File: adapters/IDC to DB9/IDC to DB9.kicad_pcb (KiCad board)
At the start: 2 copper layers, 22.9 x 18.4 mm, 2 parts, among them J1 JoyKEY, J2 DB9

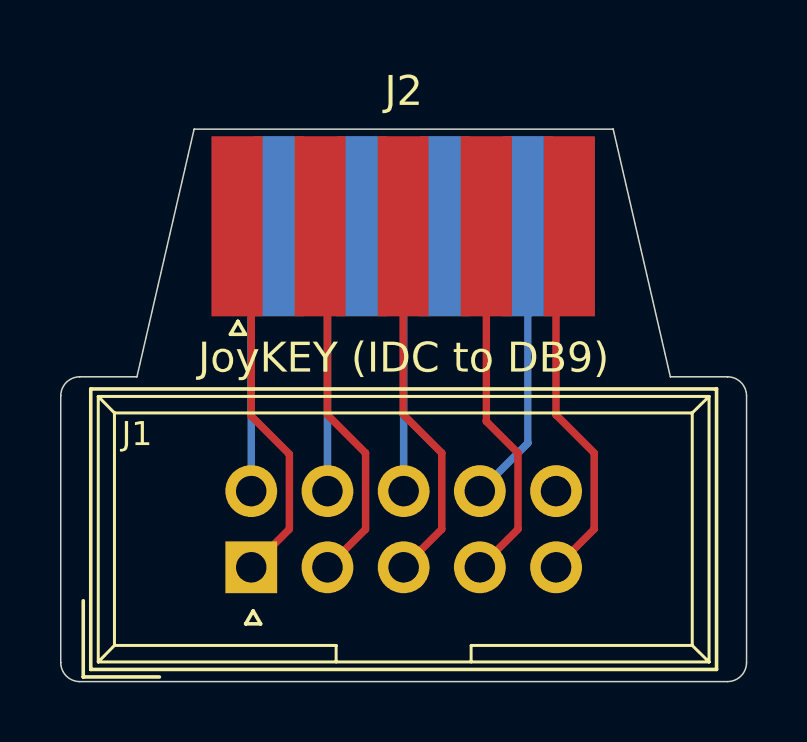
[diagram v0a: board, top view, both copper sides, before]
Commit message: Added VCC_EN to IDC -> DB9 adapter
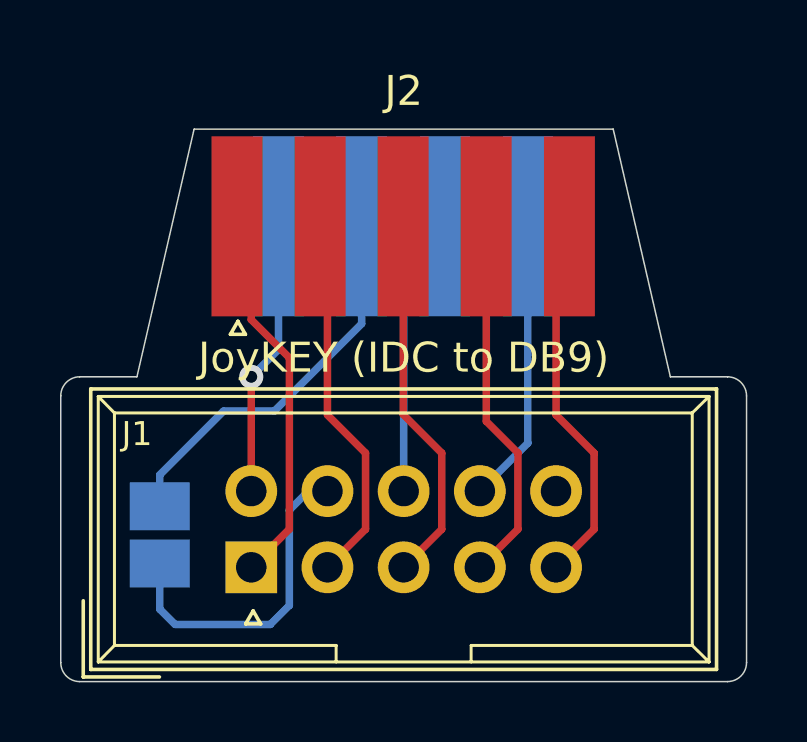
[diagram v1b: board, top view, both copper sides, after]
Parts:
- added JP1: PWR, solder_bridge:bridge, B.Cu at (134.1, 89.4)
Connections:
- J1 pad 7: VCC -> Net-(J1-Pad7)
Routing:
- net Net-(J1-Pad7): track 0.00 -> 11.0 mm
- net VCC: track 9.30 -> 13.1 mm
- net /FIRE1: vias 0 -> 1
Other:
- board text added: "VCC_EN"
- board text removed: "JoyKEY"
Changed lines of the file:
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@@
     (thickness 1.6)
     (drawings 15)
-    (tracks 31)
+    (tracks 43)
     (zones 0)
-    (modules 2)
-    (nets 10)
+    (modules 3)
+    (nets 11)
   )
   (page A4)
@@
   (net 8 /FIRE1)
   (net 9 /FIRE3)
+  (net 10 "Net-(J1-Pad7)")
   (net_class Default "This is the default net class."
     (clearance 0.2)
@@
     (add_net /UP)
     (add_net GND)
+    (add_net "Net-(J1-Pad7)")
     (add_net VCC)
   )
@@
       (net 1 GND))
     (pad 7 thru_hole oval (at 2.54 2.54 90) (size 1.7272 1.7272) (drill 1.016) (layers *.Cu *.Mask)
-      (net 7 VCC))
+      (net 10 "Net-(J1-Pad7)"))
     (pad 6 thru_hole oval (at 2.54 0 90) (size 1.7272 1.7272) (drill 1.016) (layers *.Cu *.Mask)
       (net 8 /FIRE1))
@@
     )
   )
+  (module solder_bridge:bridge (layer B.Cu)
+    (at 134.112 89.408)
+    (descr "Through hole straight pin header, 1x02, 1.00mm pitch, single row")
+    (tags "Through hole pin header THT 1x02 1.00mm single row")
+    (fp_text reference JP1 (at 0 2.54) (layer B.SilkS) hide
+      (effects (font (size 1 1) (thickness 0.15)) (justify mirror))
+    )
+    (fp_text value PWR (at 0 -2.56) (layer B.Fab)
+      (effects (font (size 1 1) (thickness 0.15)) (justify mirror))
+    )
+    (fp_text user %R (at 0 -3.81 180) (layer B.Fab)
+      (effects (font (size 0.76 0.76) (thickness 0.114)) (justify mirror))
+    )
+    (pad 1 smd rect (at 0 0) (size 2 1.6) (layers B.Cu B.Paste B.Mask)
+      (net 10 "Net-(J1-Pad7)"))
+    (pad 2 smd rect (at 0 -1.905) (size 2 1.6) (layers B.Cu B.Paste B.Mask)
+      (net 7 VCC))
+    (model ${KISYS3DMOD}/Pin_Headers.3dshapes/Pin_Header_Straight_1x02_Pitch1.00mm.wrl
+      (at (xyz 0 0 0))
+      (scale (xyz 1 1 1))
+      (rotate (xyz 0 0 0))
+    )
+  )
+  (gr_text VCC_EN (at 132.334 88.4555 90) (layer B.SilkS)
+    (effects (font (size 0.8 0.8) (thickness 0.1)) (justify mirror))
+  )
   (gr_text "IDC to DB9" (at 142.24 92.075) (layer B.SilkS)
-    (effects (font (size 0.8 0.8) (thickness 0.1)) (justify mirror))
-  )
-  (gr_text JoyKEY (at 147.32 83.82 270) (layer B.SilkS)
     (effects (font (size 0.8 0.8) (thickness 0.1)) (justify mirror))
   )
@@
   (gr_line (start 130.81 92.71) (end 130.81 83.82) (layer Edge.Cuts) (width 0.05))
   (gr_line (start 153.035 93.345) (end 131.445 93.345) (layer Edge.Cuts) (width 0.05))
-  (segment (start 142.24 79.538) (end 143.6095 78.1685) (width 0.25) (layer B.Cu) (net 1))
-  (segment (start 142.24 86.995) (end 142.24 79.538) (width 0.25) (layer B.Cu) (net 1))
+  (segment (start 142.24 79.538) (end 143.6095 78.1685) (width 0.25) (layer B.Cu) (net 1) (status 20))
+  (segment (start 142.24 86.995) (end 142.24 79.538) (width 0.25) (layer B.Cu) (net 1) (status 10))
   (segment (start 137.16 78.644) (end 136.6845 78.1685) (width 0.25) (layer F.Cu) (net 2))
-  (segment (start 137.16 84.492375) (end 137.16 78.644) (width 0.25) (layer F.Cu) (net 2))
-  (segment (start 138.43 85.762375) (end 137.16 84.492375) (width 0.25) (layer F.Cu) (net 2))
-  (segment (start 138.43 88.265) (end 138.43 85.762375) (width 0.25) (layer F.Cu) (net 2))
+  (segment (start 137.16 81.28) (end 137.16 78.644) (width 0.25) (layer F.Cu) (net 2))
+  (segment (start 138.43 82.55) (end 137.16 81.28) (width 0.25) (layer F.Cu) (net 2))
+  (segment (start 138.43 88.265) (end 138.43 82.55) (width 0.25) (layer F.Cu) (net 2))
   (segment (start 137.16 89.535) (end 138.43 88.265) (width 0.25) (layer F.Cu) (net 2))
-  (segment (start 140.97 88.265) (end 139.7 89.535) (width 0.25) (layer F.Cu) (net 3))
+  (segment (start 140.97 88.265) (end 139.7 89.535) (width 0.25) (layer F.Cu) (net 3) (status 20))
   (segment (start 140.97 85.725) (end 140.97 88.265) (width 0.25) (layer F.Cu) (net 3))
   (segment (start 139.7 84.455) (end 140.97 85.725) (width 0.25) (layer F.Cu) (net 3))
-  (segment (start 139.7 78.414) (end 139.7 84.455) (width 0.25) (layer F.Cu) (net 3))
-  (segment (start 139.4545 78.1685) (end 139.7 78.414) (width 0.25) (layer F.Cu) (net 3))
-  (segment (start 143.51 88.265) (end 142.24 89.535) (width 0.25) (layer F.Cu) (net 4))
+  (segment (start 139.7 78.414) (end 139.7 84.455) (width 0.25) (layer F.Cu) (net 3) (status 10))
+  (segment (start 139.4545 78.1685) (end 139.7 78.414) (width 0.25) (layer F.Cu) (net 3) (status 30))
+  (segment (start 143.51 88.265) (end 142.24 89.535) (width 0.25) (layer F.Cu) (net 4) (status 20))
   (segment (start 143.51 85.725) (end 143.51 88.265) (width 0.25) (layer F.Cu) (net 4))
   (segment (start 142.2245 84.4395) (end 143.51 85.725) (width 0.25) (layer F.Cu) (net 4))
-  (segment (start 142.2245 78.1685) (end 142.2245 84.4395) (width 0.25) (layer F.Cu) (net 4))
-  (segment (start 144.9945 84.6695) (end 144.9945 78.1685) (width 0.25) (layer F.Cu) (net 5))
+  (segment (start 142.2245 78.1685) (end 142.2245 84.4395) (width 0.25) (layer F.Cu) (net 4) (status 10))
+  (segment (start 144.9945 84.6695) (end 144.9945 78.1685) (width 0.25) (layer F.Cu) (net 5) (status 20))
   (segment (start 146.05 85.725) (end 144.9945 84.6695) (width 0.25) (layer F.Cu) (net 5))
   (segment (start 146.05 88.265) (end 146.05 85.725) (width 0.25) (layer F.Cu) (net 5))
-  (segment (start 144.78 89.535) (end 146.05 88.265) (width 0.25) (layer F.Cu) (net 5))
-  (segment (start 146.3795 85.3955) (end 146.3795 78.1685) (width 0.25) (layer B.Cu) (net 6))
-  (segment (start 144.78 86.995) (end 146.3795 85.3955) (width 0.25) (layer B.Cu) (net 6))
-  (segment (start 139.7 79.308) (end 140.8395 78.1685) (width 0.25) (layer B.Cu) (net 7))
-  (segment (start 139.7 86.995) (end 139.7 79.308) (width 0.25) (layer B.Cu) (net 7))
-  (segment (start 137.16 79.078) (end 138.0695 78.1685) (width 0.25) (layer B.Cu) (net 8))
-  (segment (start 137.16 86.995) (end 137.16 79.078) (width 0.25) (layer B.Cu) (net 8))
-  (segment (start 148.59 88.265) (end 147.32 89.535) (width 0.25) (layer F.Cu) (net 9))
+  (segment (start 144.78 89.535) (end 146.05 88.265) (width 0.25) (layer F.Cu) (net 5) (status 10))
+  (segment (start 146.3795 85.3955) (end 146.3795 78.1685) (width 0.25) (layer B.Cu) (net 6) (status 20))
+  (segment (start 144.78 86.995) (end 146.3795 85.3955) (width 0.25) (layer B.Cu) (net 6) (status 10))
+  (segment (start 140.8395 81.4185) (end 140.8395 78.1685) (width 0.25) (layer B.Cu) (net 7))
+  (segment (start 134.112 86.453) (end 136.237 84.328) (width 0.25) (layer B.Cu) (net 7))
+  (segment (start 137.93 84.328) (end 140.8395 81.4185) (width 0.25) (layer B.Cu) (net 7))
+  (segment (start 134.112 87.503) (end 134.112 86.453) (width 0.25) (layer B.Cu) (net 7))
+  (segment (start 136.237 84.328) (end 137.93 84.328) (width 0.25) (layer B.Cu) (net 7))
+  (segment (start 138.0695 82.2755) (end 137.16 83.185) (width 0.25) (layer B.Cu) (net 8))
+  (segment (start 138.0695 78.1685) (end 138.0695 82.2755) (width 0.25) (layer B.Cu) (net 8))
+  (segment (start 137.16 86.995) (end 137.16 83.185) (width 0.25) (layer F.Cu) (net 8))
+  (via (at 137.16 83.185) (size 0.8) (drill 0.4) (layers F.Cu B.Cu) (net 8))
+  (segment (start 148.59 88.265) (end 147.32 89.535) (width 0.25) (layer F.Cu) (net 9) (status 20))
   (segment (start 148.59 85.725) (end 148.59 88.265) (width 0.25) (layer F.Cu) (net 9))
   (segment (start 147.32 84.455) (end 148.59 85.725) (width 0.25) (layer F.Cu) (net 9))
-  (segment (start 147.32 78.613) (end 147.32 84.455) (width 0.25) (layer F.Cu) (net 9))
-  (segment (start 147.7645 78.1685) (end 147.32 78.613) (width 0.25) (layer F.Cu) (net 9))
+  (segment (start 147.32 78.613) (end 147.32 84.455) (width 0.25) (layer F.Cu) (net 9) (status 10))
+  (segment (start 147.7645 78.1685) (end 147.32 78.613) (width 0.25) (layer F.Cu) (net 9) (status 30))
+  (segment (start 134.112 90.932) (end 134.112 89.408) (width 0.25) (layer B.Cu) (net 10))
+  (segment (start 134.62 91.44) (end 134.112 90.932) (width 0.25) (layer B.Cu) (net 10))
+  (segment (start 137.795 91.44) (end 134.62 91.44) (width 0.25) (layer B.Cu) (net 10))
+  (segment (start 138.43 90.805) (end 137.795 91.44) (width 0.25) (layer B.Cu) (net 10))
+  (segment (start 138.43 87.63) (end 138.43 90.805) (width 0.25) (layer B.Cu) (net 10))
+  (segment (start 139.065 86.995) (end 138.43 87.63) (width 0.25) (layer B.Cu) (net 10))
+  (segment (start 139.7 86.995) (end 139.065 86.995) (width 0.25) (layer B.Cu) (net 10))
 )
